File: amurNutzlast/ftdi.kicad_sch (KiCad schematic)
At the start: 7 parts, among them U4 FT2232HL, U5 93LCxxA

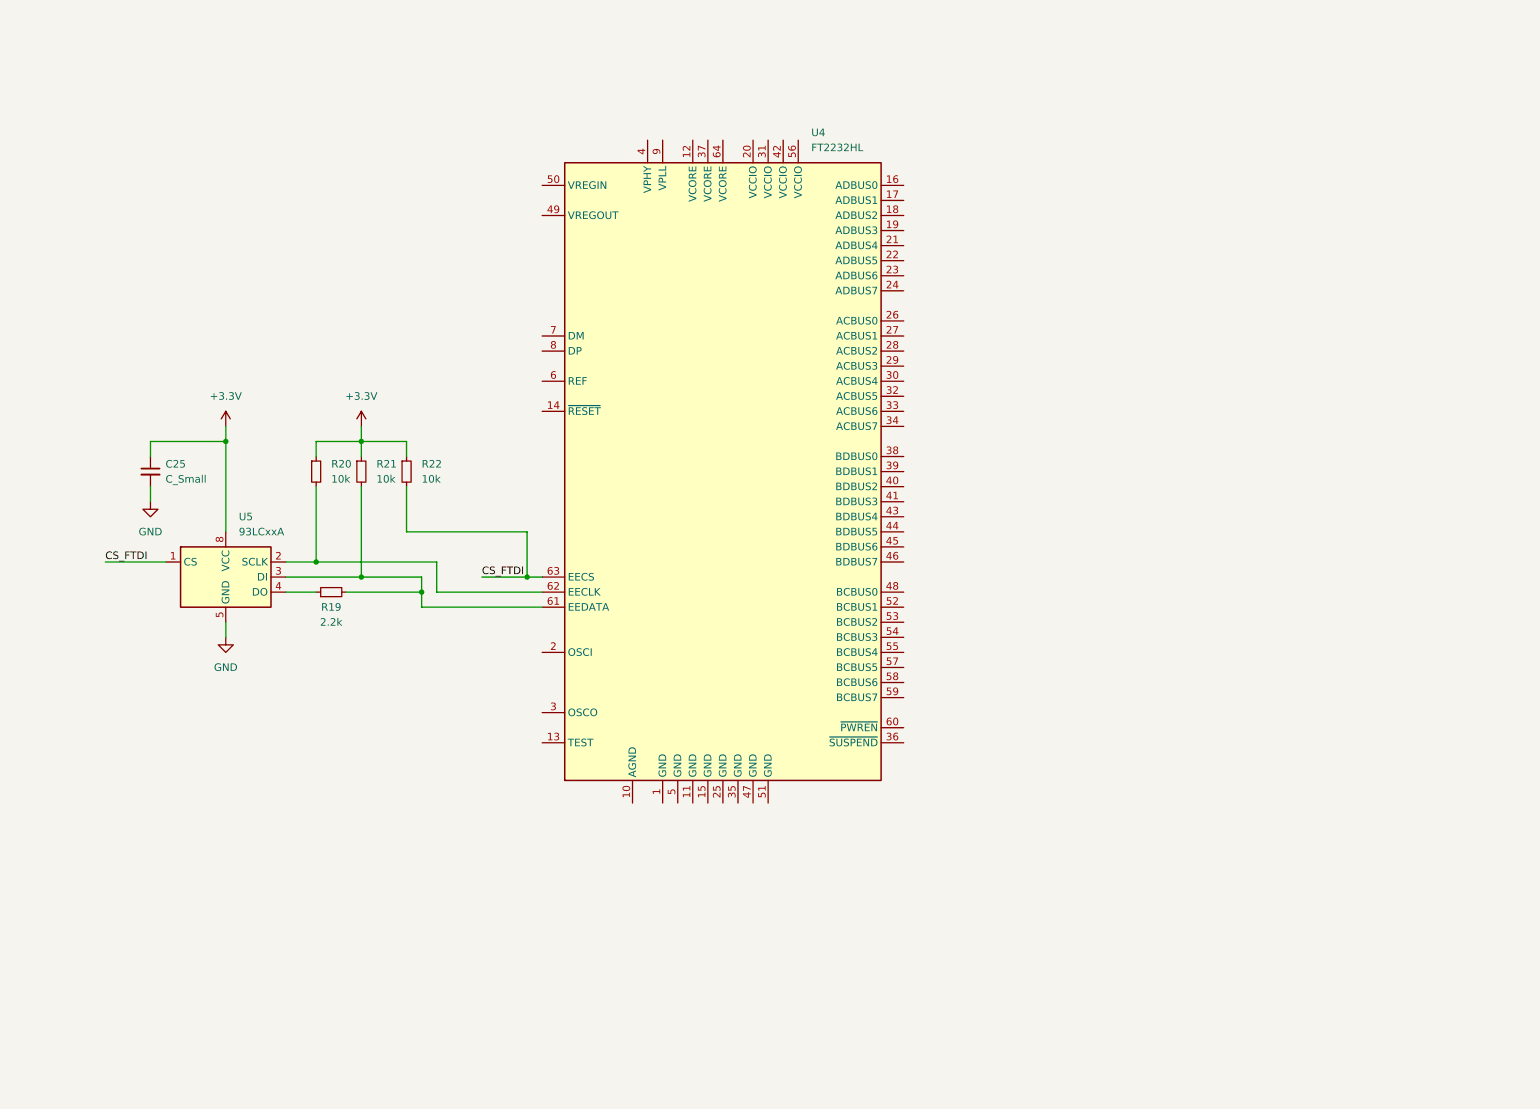
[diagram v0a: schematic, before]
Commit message: ftdi schematic was added apart of the USB
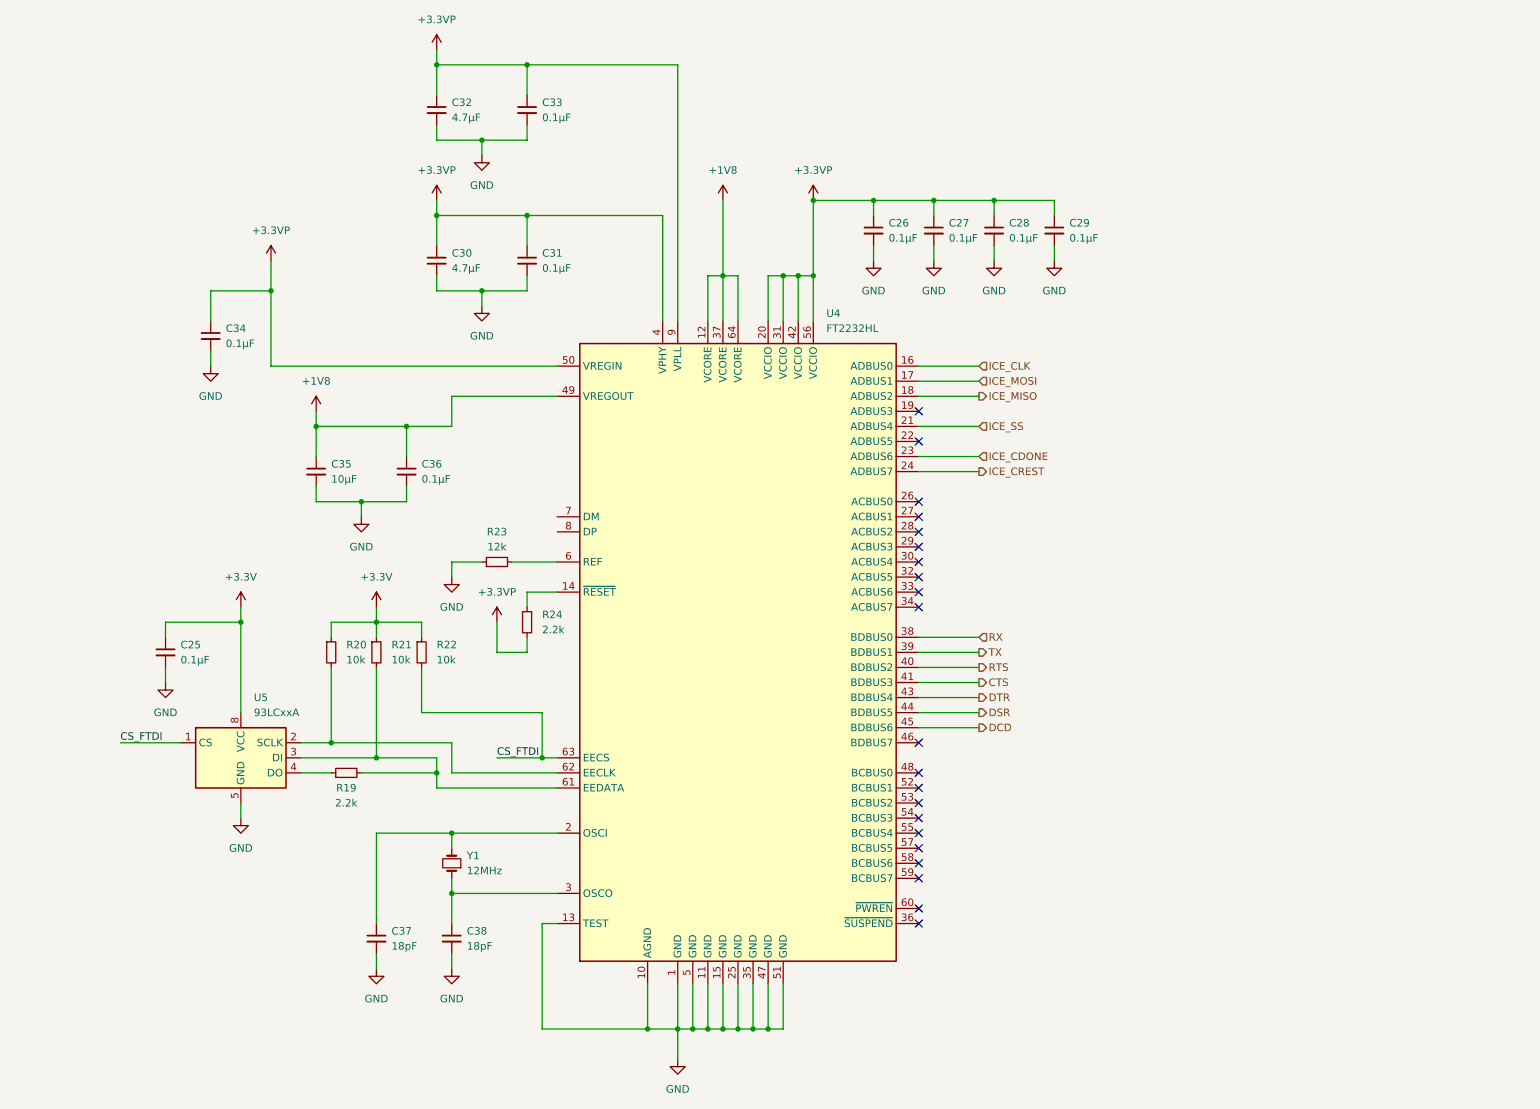
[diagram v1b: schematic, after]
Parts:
- added C26, C27, C28, C29, C31, C33, C34, C36: 0.1µF, symbol Device:C_Small
- added C30, C32: 4.7µF, symbol Device:C_Small
- added C35: 10µF, symbol Device:C_Small
- added C37, C38: 18pF, symbol Device:C_Small
- added R23: 12k, symbol Device:R_Small
- added R24: 2.2k, symbol Device:R_Small
- added Y1: 12MHz, symbol Device:Crystal_Small
- C25: value C_Small -> 0.1µF
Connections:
- net GND: now also U4.1 (GND), U4.10 (AGND), U4.11 (GND), U4.13 (TEST), U4.15 (GND), U4.25 (GND), U4.35 (GND), U4.47 (GND), U4.5 (GND), U4.51 (GND), C26.2, C27.2, C28.2, C29.2, C30.2, C31.2, C32.2, C33.2, C34.2, C35.2, C36.2, C37.2, C38.2, R23.1
- net +1V8: now reaches U4.12 (VCORE)
- net +1V8: now also U4.37 (VCORE), U4.49 (VREGOUT), U4.64 (VCORE), C35.1, C36.1
- net at U4.14 (~{RESET}): now also R24.1
- net ICE_CLK: now reaches U4.16 (ADBUS0)
- net ICE_MOSI: now reaches U4.17 (ADBUS1)
- net ICE_MISO: now reaches U4.18 (ADBUS2)
- net at U4.2 (OSCI): now also C37.1, Y1.2
- net +3.3VP: now reaches U4.20 (VCCIO)
- net +3.3VP: now also U4.31 (VCCIO), U4.4 (VPHY), U4.42 (VCCIO), U4.50 (VREGIN), U4.56 (VCCIO), U4.9 (VPLL), C26.1, C27.1, C28.1, C29.1, C30.1, C31.1, C32.1, C33.1, C34.1, R24.2
- net ICE_SS: now reaches U4.21 (ADBUS4)
- net ICE_CDONE: now reaches U4.23 (ADBUS6)
- net ICE_CREST: now reaches U4.24 (ADBUS7)
- net at U4.3 (OSCO): now also C38.1, Y1.1
- net RX: now reaches U4.38 (BDBUS0)
- net TX: now reaches U4.39 (BDBUS1)
- net RTS: now reaches U4.40 (BDBUS2)
- net CTS: now reaches U4.41 (BDBUS3)
- net DTR: now reaches U4.43 (BDBUS4)
- net DSR: now reaches U4.44 (BDBUS5)
- net DCD: now reaches U4.45 (BDBUS6)
- net at U4.6 (REF): now also R23.2
- no-connect marks 0 -> 21
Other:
- moved on the sheet: C25, R19, R20, R21, R22, U4, U5

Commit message: finisched design schematics + pdf
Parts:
- added C39, C40: 0.1µF, symbol Device:C_Small
- added C41: 10µF, symbol Device:C_Small
- added D5: LED_Small, symbol Device:LED_Small
- added J2: USB_A, symbol Connector:USB_A
- added R25: 500, symbol Device:R_Small
- added U3: LD1117S33TR_SOT223, Package_TO_SOT_SMD:SOT-223-3_TabPin2, symbol Regulator_Linear:LD1117S33TR_SOT223
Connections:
- net +3.3VP: now also C41.1, U3.2 (VO)
- net GND: now also C39.2, C40.2, C41.2, D5.1 (K), J2.4 (GND), J2.5 (Shield), U3.1 (GND)
- net DM: now reaches U4.7 (DM)
- net DM: now also J2.2 (D-)
- net DP: now reaches U4.8 (DP)
- net DP: now also J2.3 (D+)
- new net: D5.2 (A), R25.2
- new net VBUS: C39.1, C40.1, J2.1 (VBUS), R25.1, U3.3 (VI)

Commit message: layout start
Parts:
- C25, C26, C27, C28, C29, C30, C31, C32, C33, C34, C35, C36, C37, C38, C39, C40, C41: footprint (none) -> Capacitor_SMD:C_0603_1608Metric
- D5: footprint (none) -> LED_SMD:LED_0603_1608Metric
- J2: footprint (none) -> Connector_USB:USB_A_CNCTech_1001-011-01101_Horizontal
- R19, R20, R21, R22, R23, R24, R25: footprint (none) -> Resistor_SMD:R_0603_1608Metric
- U5: footprint (none) -> Package_SO:SOIC-8_3.9x4.9mm_P1.27mm
- Y1: footprint (none) -> Crystal:Crystal_SMD_HC49-SD_HandSoldering
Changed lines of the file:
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@@
       (effects (font (size 1.27 1.27)) (justify left))
     )
-    (property "Footprint" "" (at 20.32 73.66 0)
+    (property "Footprint" "Resistor_SMD:R_0603_1608Metric" (at 20.32 73.66 0)
       (effects (font (size 1.27 1.27)) hide)
     )
@@
       (effects (font (size 1.27 1.27)))
     )
-    (property "Footprint" "" (at 71.12 142.24 0)
+    (property "Footprint" "Resistor_SMD:R_0603_1608Metric" (at 71.12 142.24 0)
       (effects (font (size 1.27 1.27)) hide)
     )
@@
       (effects (font (size 1.27 1.27)) (justify left))
     )
-    (property "Footprint" "" (at 101.6 30.48 0)
+    (property "Footprint" "Capacitor_SMD:C_0603_1608Metric" (at 101.6 30.48 0)
       (effects (font (size 1.27 1.27)) hide)
     )
@@
       (effects (font (size 1.27 1.27)))
     )
-    (property "Footprint" "" (at 29.21 105.41 0)
-      (effects (font (size 1.27 1.27)) hide)
-    )
-    (property "Datasheet" " ~" (at 29.21 105.41 0)
+    (property "Footprint" "Connector_USB:USB_A_CNCTech_1001-011-01101_Horizontal" (at 29.21 105.41 0)
+      (effects (font (size 1.27 1.27)) hide)
+    )
+    (property "Datasheet" "https://www.mouser.de/ProductDetail/Molex/48037-2200?qs=naUSJSqnqcIBwHMiwQ2VeA%3D%3D" (at 29.21 105.41 0)
       (effects (font (size 1.27 1.27)) hide)
     )
@@
       (effects (font (size 1.27 1.27)) (justify left))
     )
-    (property "Footprint" "" (at 81.28 91.44 0)
+    (property "Footprint" "Capacitor_SMD:C_0603_1608Metric" (at 81.28 91.44 0)
       (effects (font (size 1.27 1.27)) hide)
     )
@@
       (effects (font (size 1.27 1.27)) (justify left))
     )
-    (property "Footprint" "" (at 40.64 88.9 0)
+    (property "Footprint" "Capacitor_SMD:C_0603_1608Metric" (at 40.64 88.9 0)
       (effects (font (size 1.27 1.27)) hide)
     )
@@
       (effects (font (size 1.27 1.27)) (justify left))
     )
-    (property "Footprint" "" (at 88.9 170.18 0)
+    (property "Footprint" "Capacitor_SMD:C_0603_1608Metric" (at 88.9 170.18 0)
       (effects (font (size 1.27 1.27)) hide)
     )
@@
       (effects (font (size 1.27 1.27)) (justify right))
     )
-    (property "Footprint" "" (at 20.32 81.28 90)
+    (property "Footprint" "LED_SMD:LED_0603_1608Metric" (at 20.32 81.28 90)
       (effects (font (size 1.27 1.27)) hide)
     )
@@
       (effects (font (size 1.27 1.27)) (justify left))
     )
-    (property "Footprint" "" (at 180.34 50.8 0)
+    (property "Footprint" "Capacitor_SMD:C_0603_1608Metric" (at 180.34 50.8 0)
       (effects (font (size 1.27 1.27)) hide)
     )
@@
       (effects (font (size 1.27 1.27)) (justify left))
     )
-    (property "Footprint" "" (at 101.6 116.84 0)
+    (property "Footprint" "Resistor_SMD:R_0603_1608Metric" (at 101.6 116.84 0)
       (effects (font (size 1.27 1.27)) hide)
     )
@@
       (effects (font (size 1.27 1.27)) (justify left))
     )
-    (property "Footprint" "" (at 76.2 170.18 0)
+    (property "Footprint" "Capacitor_SMD:C_0603_1608Metric" (at 76.2 170.18 0)
       (effects (font (size 1.27 1.27)) hide)
     )
@@
       (effects (font (size 1.27 1.27)) (justify left))
     )
-    (property "Footprint" "" (at 48.26 68.58 0)
+    (property "Footprint" "Capacitor_SMD:C_0603_1608Metric" (at 48.26 68.58 0)
       (effects (font (size 1.27 1.27)) hide)
     )
@@
       (effects (font (size 1.27 1.27)) (justify left))
     )
-    (property "Footprint" "" (at 261.62 96.52 0)
+    (property "Footprint" "Capacitor_SMD:C_0603_1608Metric" (at 261.62 96.52 0)
       (effects (font (size 1.27 1.27)) hide)
     )
@@
       (effects (font (size 1.27 1.27)) (justify left))
     )
-    (property "Footprint" "" (at 101.6 55.88 0)
+    (property "Footprint" "Capacitor_SMD:C_0603_1608Metric" (at 101.6 55.88 0)
       (effects (font (size 1.27 1.27)) hide)
     )
@@
       (effects (font (size 1.27 1.27)) (justify left))
     )
-    (property "Footprint" "" (at 40.64 121.92 0)
+    (property "Footprint" "Capacitor_SMD:C_0603_1608Metric" (at 40.64 121.92 0)
       (effects (font (size 1.27 1.27)) hide)
     )
@@
       (effects (font (size 1.27 1.27)) (justify left))
     )
-    (property "Footprint" "" (at 170.18 50.8 0)
+    (property "Footprint" "Capacitor_SMD:C_0603_1608Metric" (at 170.18 50.8 0)
       (effects (font (size 1.27 1.27)) hide)
     )
@@
       (effects (font (size 1.27 1.27)) (justify left))
     )
-    (property "Footprint" "" (at 190.5 50.8 0)
+    (property "Footprint" "Capacitor_SMD:C_0603_1608Metric" (at 190.5 50.8 0)
       (effects (font (size 1.27 1.27)) hide)
     )
@@
       (effects (font (size 1.27 1.27)) (justify left))
     )
-    (property "Footprint" "" (at 68.58 121.92 0)
+    (property "Footprint" "Resistor_SMD:R_0603_1608Metric" (at 68.58 121.92 0)
       (effects (font (size 1.27 1.27)) hide)
     )
@@
       (effects (font (size 1.27 1.27)) (justify left))
     )
-    (property "Footprint" "" (at 76.2 121.92 0)
+    (property "Footprint" "Resistor_SMD:R_0603_1608Metric" (at 76.2 121.92 0)
       (effects (font (size 1.27 1.27)) hide)
     )
@@
       (effects (font (size 1.27 1.27)) (justify right))
     )
-    (property "Footprint" "" (at 88.9 157.48 0)
+    (property "Footprint" "Crystal:Crystal_SMD_HC49-SD_HandSoldering" (at 88.9 157.48 0)
       (effects (font (size 1.27 1.27)) hide)
     )
@@
       (effects (font (size 1.27 1.27)) (justify left))
     )
-    (property "Footprint" "" (at 231.14 96.52 0)
+    (property "Footprint" "Capacitor_SMD:C_0603_1608Metric" (at 231.14 96.52 0)
       (effects (font (size 1.27 1.27)) hide)
     )
@@
       (effects (font (size 1.27 1.27)) (justify left))
     )
-    (property "Footprint" "" (at 53.34 139.7 0)
+    (property "Footprint" "Package_SO:SOIC-8_3.9x4.9mm_P1.27mm" (at 53.34 139.7 0)
       (effects (font (size 1.27 1.27)) hide)
     )
@@
       (effects (font (size 1.27 1.27)))
     )
-    (property "Footprint" "" (at 96.52 106.68 0)
+    (property "Footprint" "Resistor_SMD:R_0603_1608Metric" (at 96.52 106.68 0)
       (effects (font (size 1.27 1.27)) hide)
     )
@@
       (effects (font (size 1.27 1.27)) (justify left))
     )
-    (property "Footprint" "" (at 86.36 55.88 0)
+    (property "Footprint" "Capacitor_SMD:C_0603_1608Metric" (at 86.36 55.88 0)
       (effects (font (size 1.27 1.27)) hide)
     )
@@
       (effects (font (size 1.27 1.27)) (justify left))
     )
-    (property "Footprint" "" (at 160.02 50.8 0)
+    (property "Footprint" "Capacitor_SMD:C_0603_1608Metric" (at 160.02 50.8 0)
       (effects (font (size 1.27 1.27)) hide)
     )
@@
       (effects (font (size 1.27 1.27)) (justify left))
     )
-    (property "Footprint" "" (at 66.04 91.44 0)
+    (property "Footprint" "Capacitor_SMD:C_0603_1608Metric" (at 66.04 91.44 0)
       (effects (font (size 1.27 1.27)) hide)
     )
@@
       (effects (font (size 1.27 1.27)) (justify left))
     )
-    (property "Footprint" "" (at 83.82 121.92 0)
+    (property "Footprint" "Resistor_SMD:R_0603_1608Metric" (at 83.82 121.92 0)
       (effects (font (size 1.27 1.27)) hide)
     )
@@
       (effects (font (size 1.27 1.27)) (justify left))
     )
-    (property "Footprint" "" (at 86.36 30.48 0)
-      (effects (font (size 1.27 1.27)) hide)
-    )
+    (property "Footprint" "Capacitor_SMD:C_0603_1608Metric" (at 86.36 30.48 0)
+      (effects (font (size 1.27 1.27)) hide)
+    )
